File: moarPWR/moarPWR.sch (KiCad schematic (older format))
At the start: 0 parts

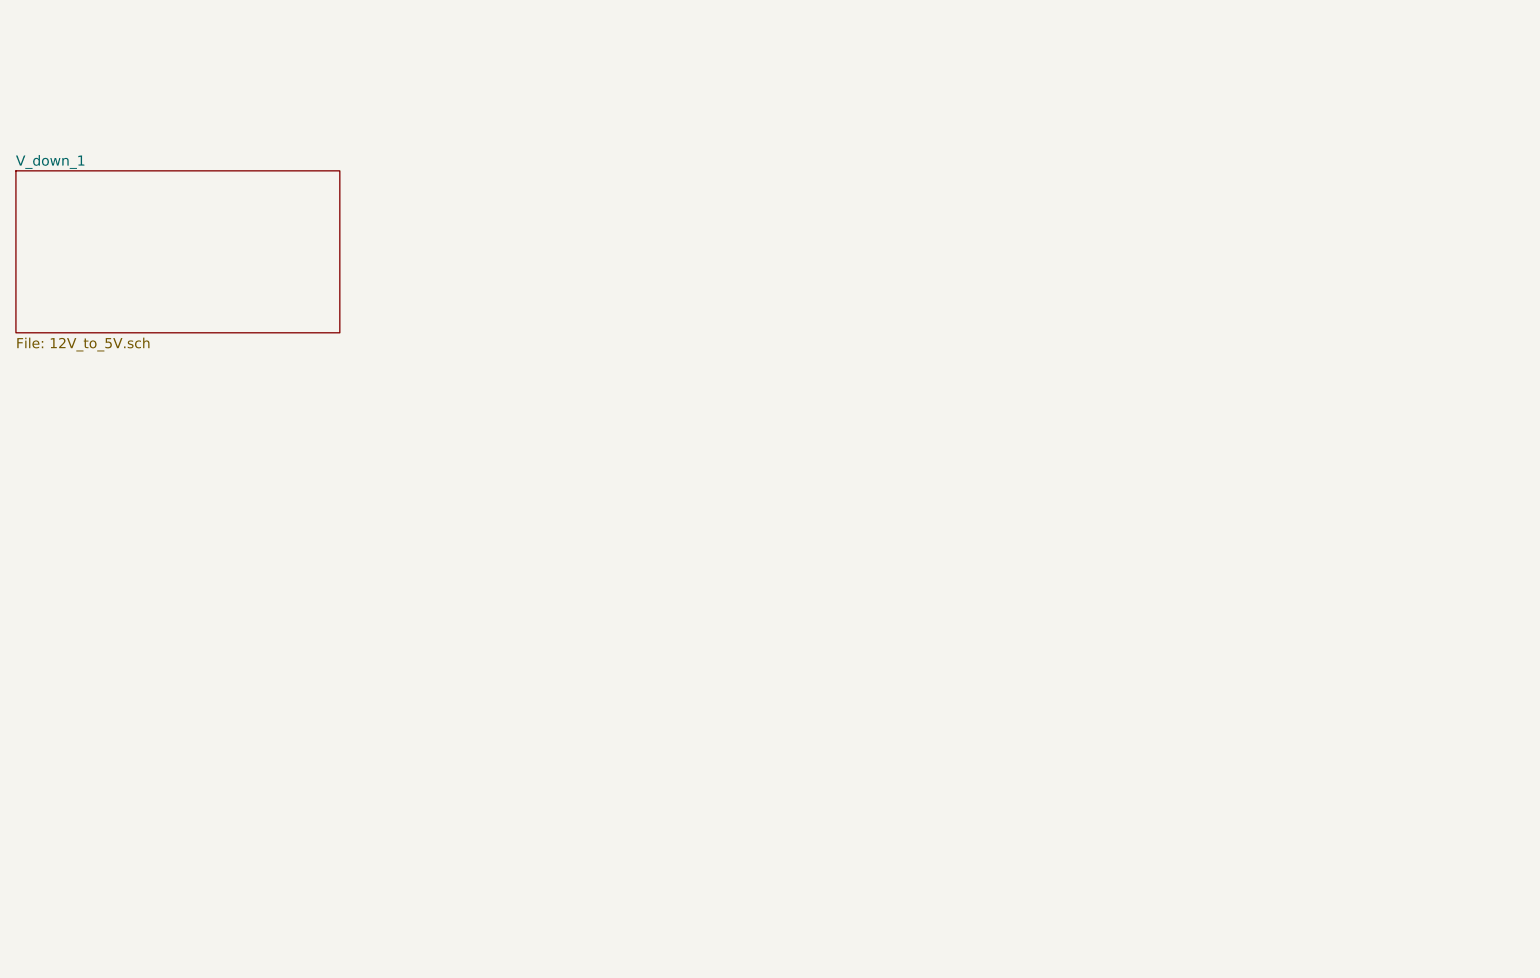
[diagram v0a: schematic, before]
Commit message: Added 5V stepdown skeleton and fleshed out top level sheet
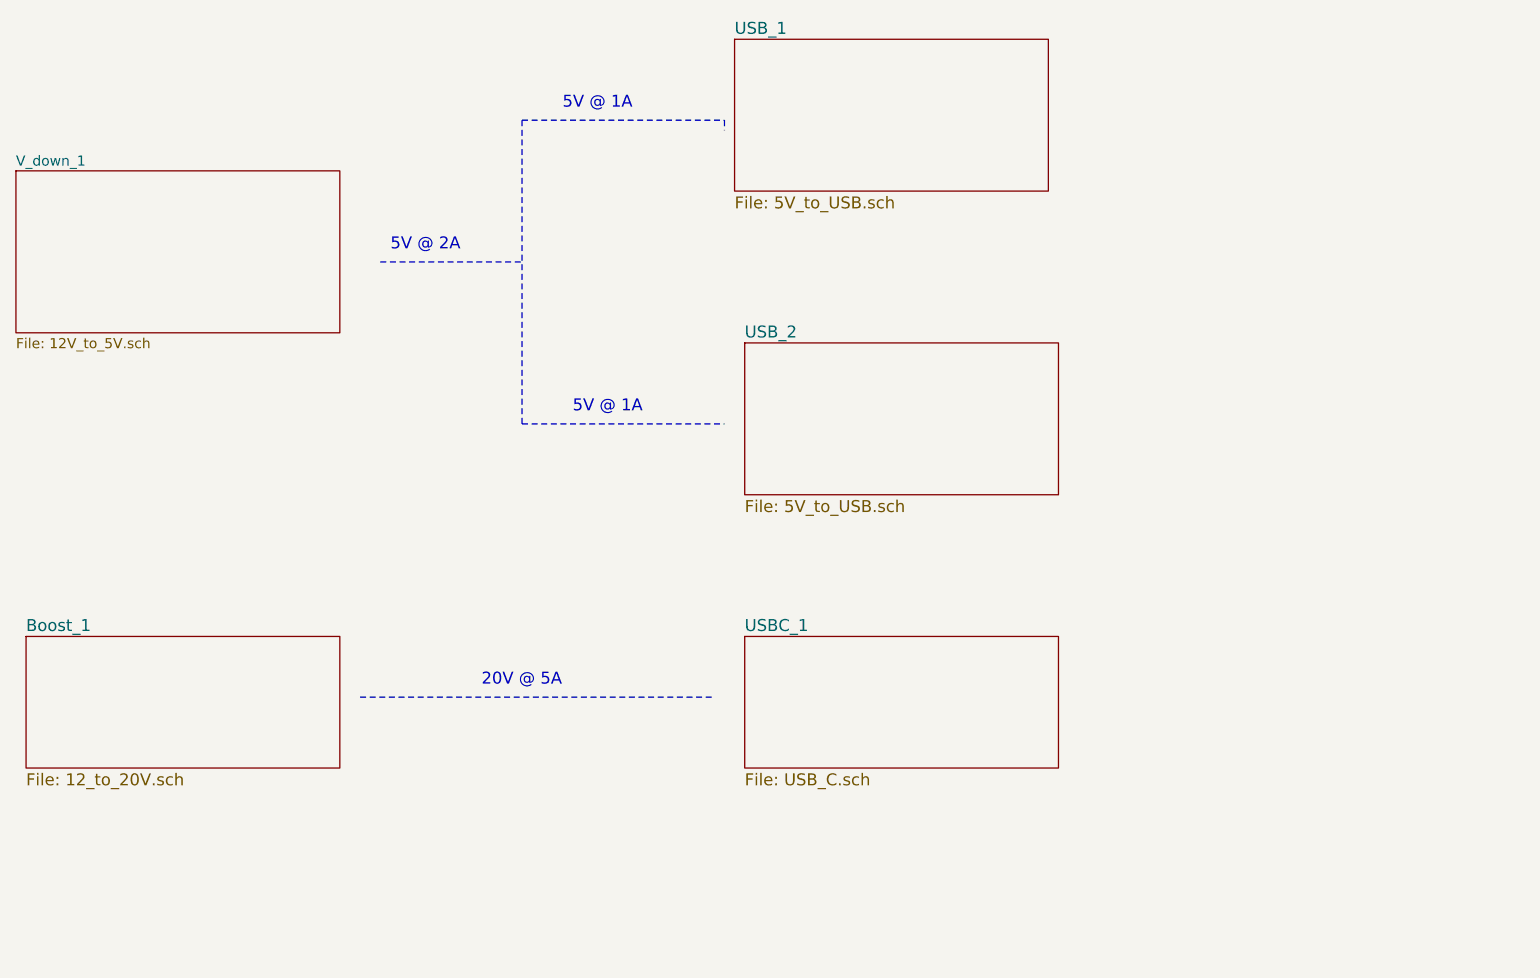
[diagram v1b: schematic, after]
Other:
- note added: "20V @ 5A"
- note added: "5V @ 1A"
- note added: "5V @ 2A"
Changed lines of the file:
@@
 EESchema Schematic File Version 4
+LIBS:moarPWR-cache
 EELAYER 26 0
 EELAYER END
 $Descr A4 11693 8268
 encoding utf-8
-Sheet 1 2
+Sheet 1 5
 Title "moarPWR"
 Date ""
@@
 F1 "12V_to_5V.sch" 50
 $EndSheet
+$Sheet
+S 5050 1850 1550 750
+U 5B5E9C4D
+F0 "USB_1" 59
+F1 "5V_to_USB.sch" 59
+$EndSheet
+$Sheet
+S 5100 3350 1550 750
+U 5B5E9C53
+F0 "USB_2" 59
+F1 "5V_to_USB.sch" 59
+$EndSheet
+Wire Notes Line
+	3300 2950 4000 2950
+Wire Notes Line
+	4000 2250 5000 2250
+Wire Notes Line
+	5000 2250 5000 2300
+Wire Notes Line
+	4000 3750 5000 3750
+Wire Notes Line
+	4000 2250 4000 3750
+$Sheet
+S 1550 4800 1550 650
+U 5B5E9CD0
+F0 "Boost_1" 59
+F1 "12_to_20V.sch" 59
+$EndSheet
+$Sheet
+S 5100 4800 1550 650
+U 5B5E9D28
+F0 "USBC_1" 59
+F1 "USB_C.sch" 59
+$EndSheet
+Wire Notes Line
+	3200 5100 4950 5100
+Text Notes 3350 2900 0    59   ~ 0
+5V @ 2A
+Text Notes 4200 2200 0    59   ~ 0
+5V @ 1A
+Text Notes 4250 3700 0    59   ~ 0
+5V @ 1A
+Text Notes 3800 5050 0    59   ~ 0
+20V @ 5A
 $EndSCHEMATC

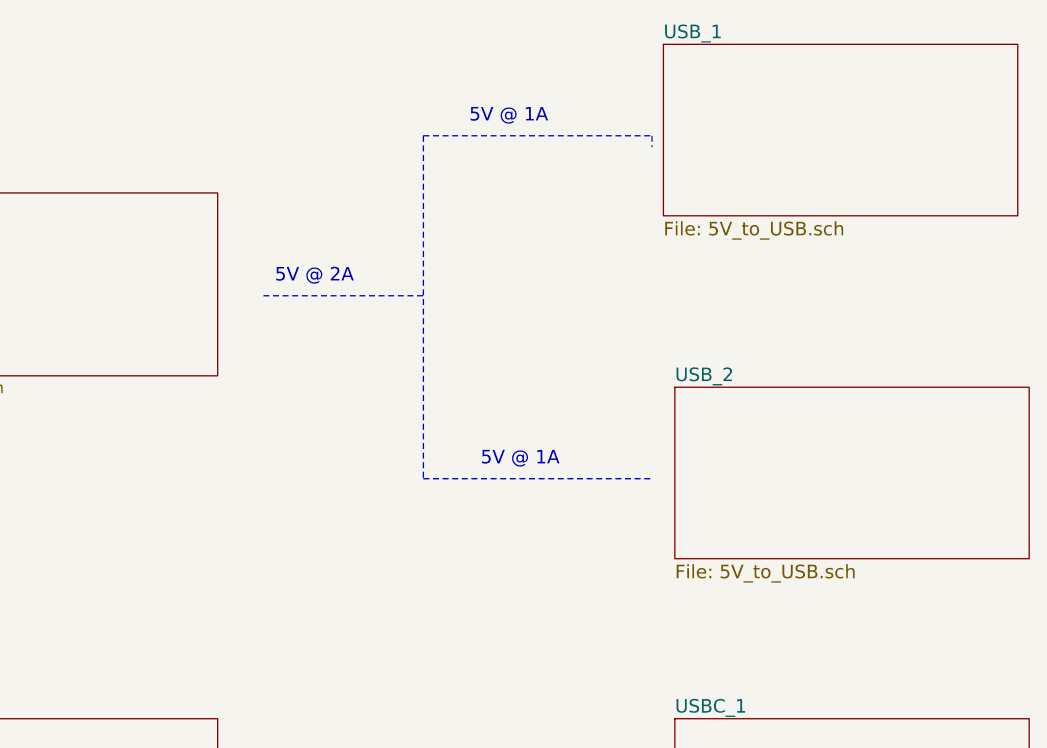
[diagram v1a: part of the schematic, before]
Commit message: Added port controller and power switch for 5V USB channels
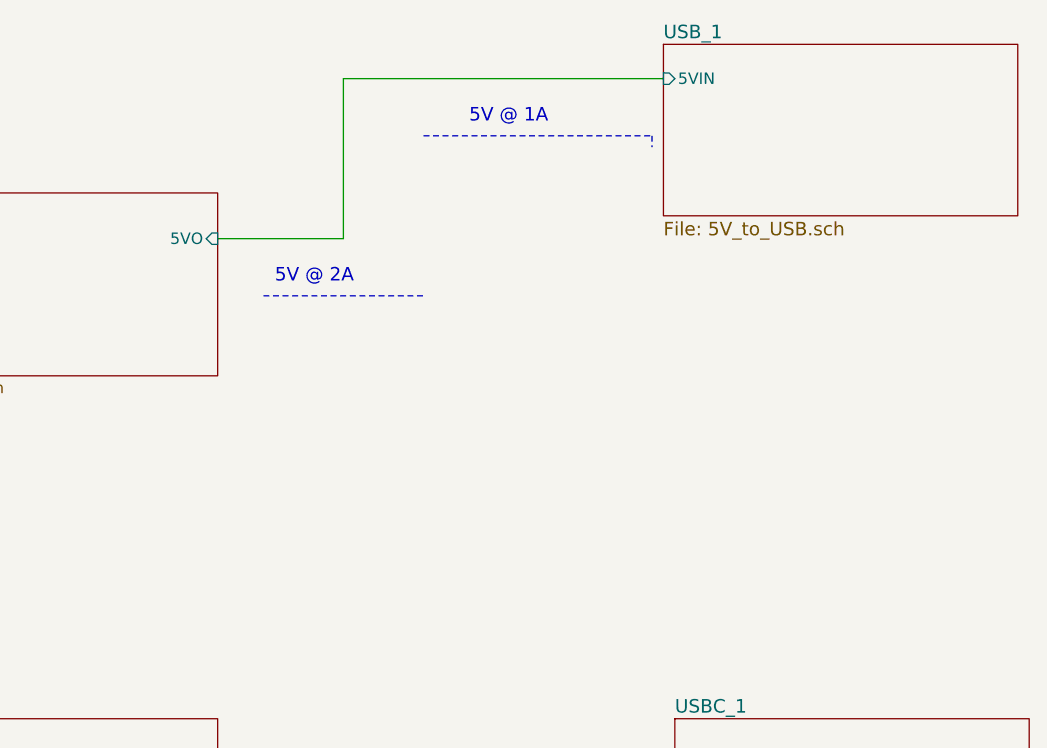
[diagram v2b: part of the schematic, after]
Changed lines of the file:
@@
 F0 "V_down_1" 50
 F1 "12V_to_5V.sch" 50
+F2 "5VO" I R 3100 2700 50
 $EndSheet
 $Sheet
@@
 F0 "USB_1" 59
 F1 "5V_to_USB.sch" 59
-$EndSheet
-$Sheet
-S 5100 3350 1550 750
-U 5B5E9C53
-F0 "USB_2" 59
-F1 "5V_to_USB.sch" 59
+F2 "5VIN" I L 5050 2000 50
 $EndSheet
 Wire Notes Line
@@
 Wire Notes Line
 	5000 2250 5000 2300
-Wire Notes Line
-	4000 3750 5000 3750
-Wire Notes Line
-	4000 2250 4000 3750
 $Sheet
 S 1550 4800 1550 650
@@
 Text Notes 4200 2200 0    59   ~ 0
 5V @ 1A
-Text Notes 4250 3700 0    59   ~ 0
-5V @ 1A
 Text Notes 3800 5050 0    59   ~ 0
 20V @ 5A
+Wire Wire Line
+	3100 2700 3650 2700
+Wire Wire Line
+	3650 2700 3650 2000
+Wire Wire Line
+	3650 2000 5050 2000
 $EndSCHEMATC

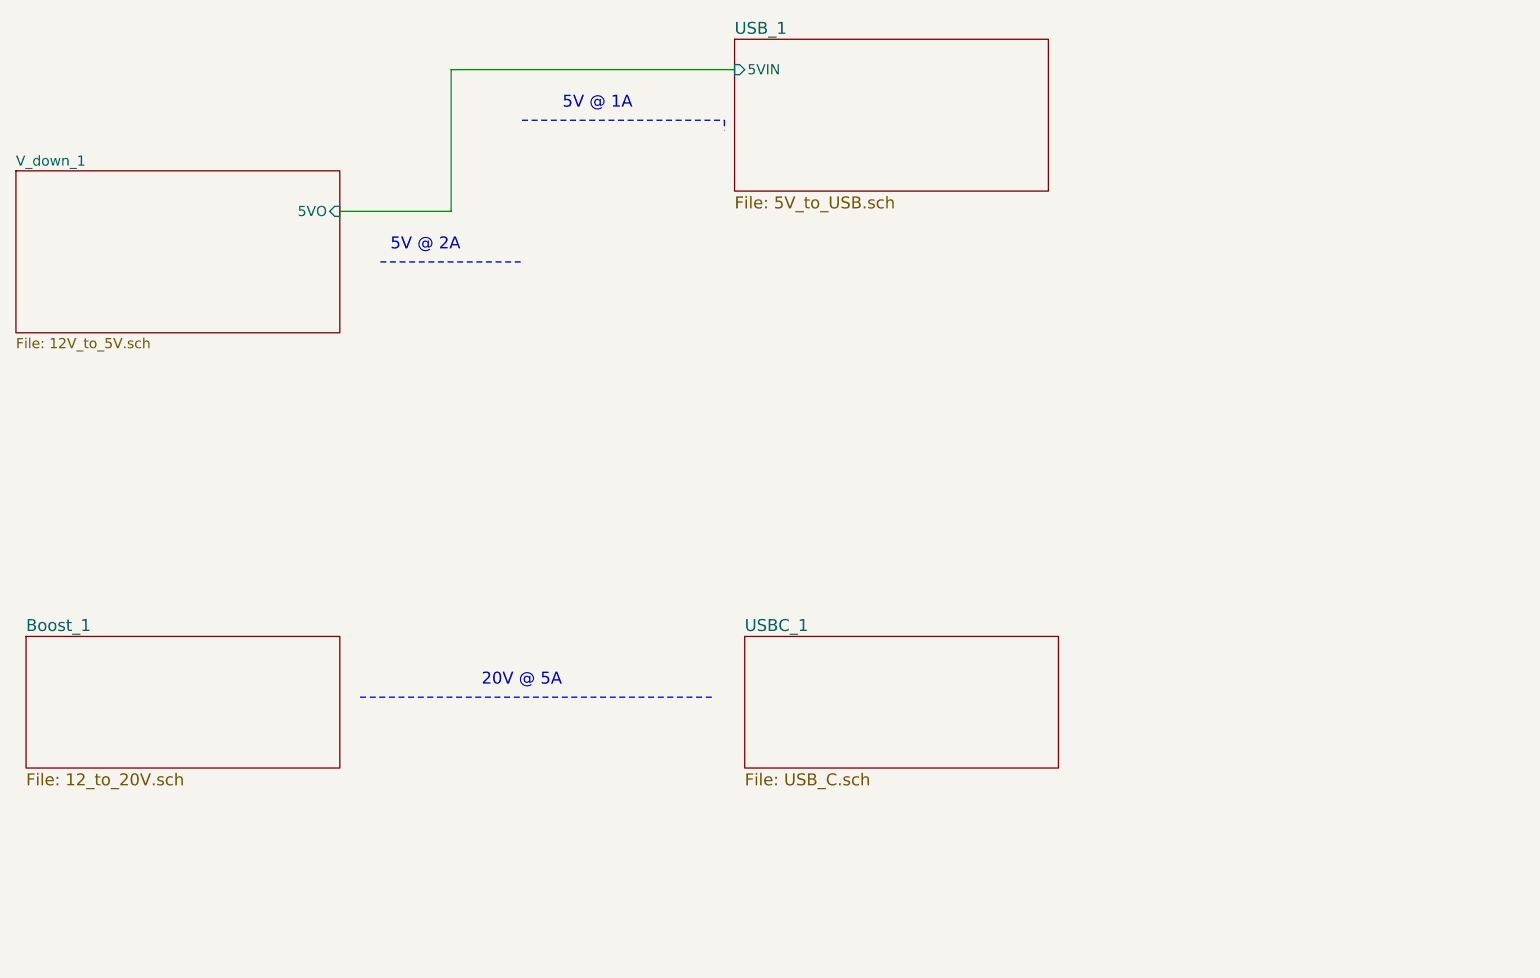
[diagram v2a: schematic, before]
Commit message: Updated part numbers in USB and display control. Added 7 Segment displays and driver.
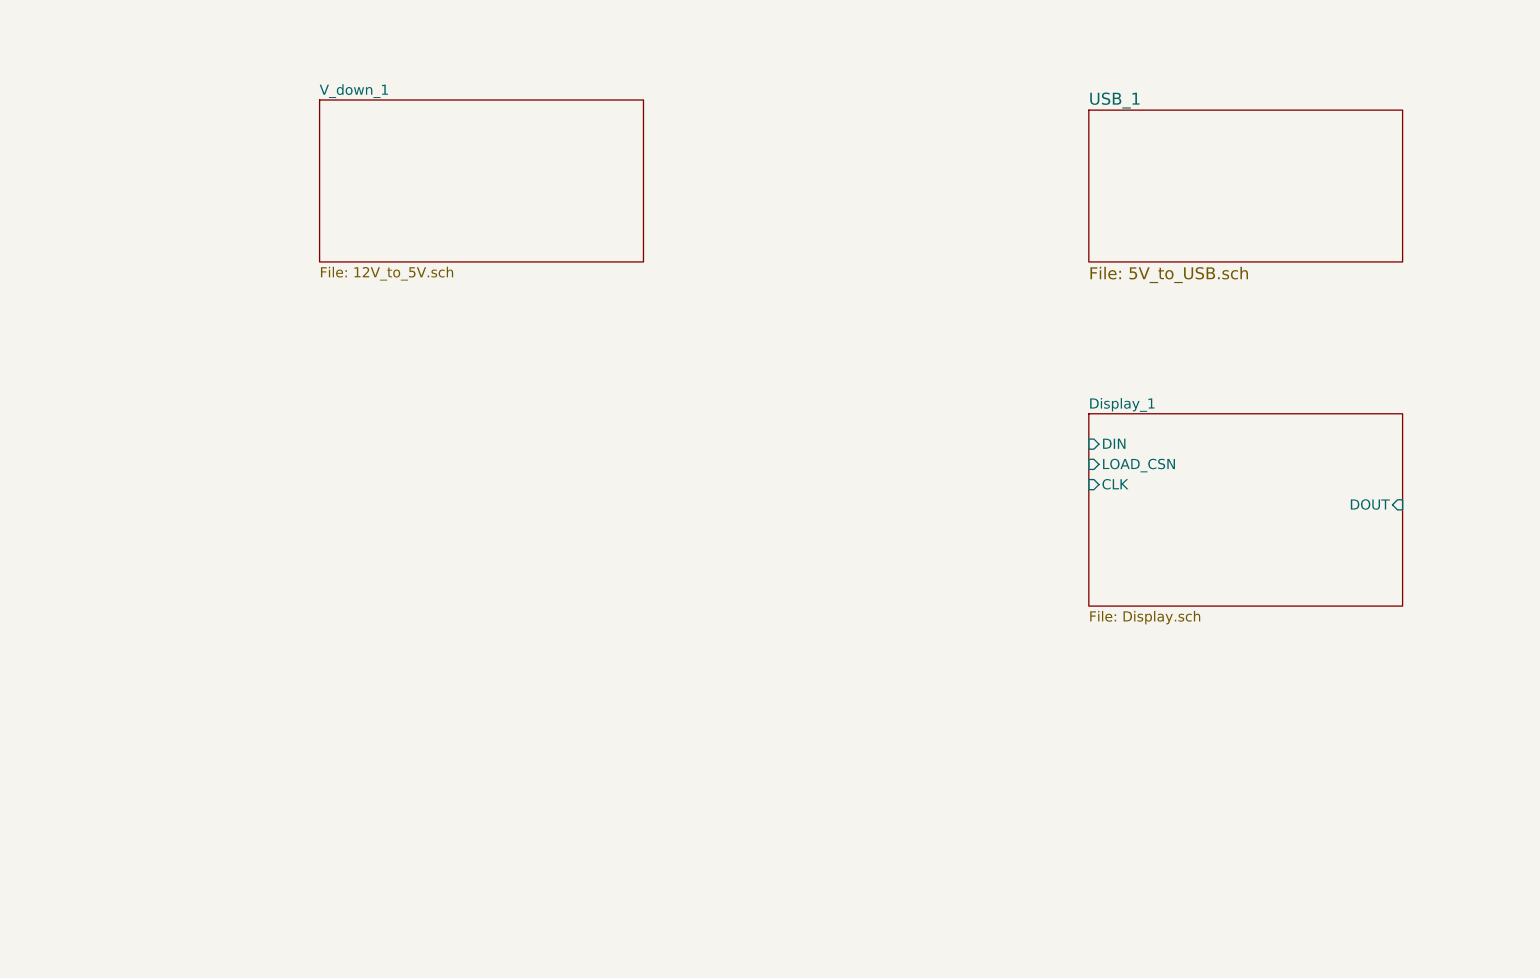
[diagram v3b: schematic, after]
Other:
- note removed: "20V @ 5A"
- note removed: "5V @ 1A"
- note removed: "5V @ 2A"
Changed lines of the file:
@@
 $Descr A4 11693 8268
 encoding utf-8
-Sheet 1 5
+Sheet 1 4
 Title "moarPWR"
 Date ""
@@
 $EndDescr
 $Sheet
-S 1500 2500 1600 800
+S 3000 2150 1600 800
 U 5B5D400A
 F0 "V_down_1" 50
 F1 "12V_to_5V.sch" 50
-F2 "5VO" I R 3100 2700 50
 $EndSheet
 $Sheet
-S 5050 1850 1550 750
+S 6800 2200 1550 750
 U 5B5E9C4D
 F0 "USB_1" 59
 F1 "5V_to_USB.sch" 59
-F2 "5VIN" I L 5050 2000 50
-$EndSheet
-Wire Notes Line
-	3300 2950 4000 2950
-Wire Notes Line
-	4000 2250 5000 2250
-Wire Notes Line
-	5000 2250 5000 2300
-$Sheet
-S 1550 4800 1550 650
-U 5B5E9CD0
-F0 "Boost_1" 59
-F1 "12_to_20V.sch" 59
 $EndSheet
 $Sheet
-S 5100 4800 1550 650
-U 5B5E9D28
-F0 "USBC_1" 59
-F1 "USB_C.sch" 59
+S 6800 3700 1550 950
+U 5BA57DA6
+F0 "Display_1" 50
+F1 "Display.sch" 50
+F2 "DIN" I L 6800 3850 50
+F3 "LOAD_CSN" I L 6800 3950 50
+F4 "CLK" I L 6800 4050 50
+F5 "DOUT" I R 8350 4150 50
 $EndSheet
-Wire Notes Line
-	3200 5100 4950 5100
-Text Notes 3350 2900 0    59   ~ 0
-5V @ 2A
-Text Notes 4200 2200 0    59   ~ 0
-5V @ 1A
-Text Notes 3800 5050 0    59   ~ 0
-20V @ 5A
-Wire Wire Line
-	3100 2700 3650 2700
-Wire Wire Line
-	3650 2700 3650 2000
-Wire Wire Line
-	3650 2000 5050 2000
 $EndSCHEMATC

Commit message: Added MSP and current sense amplifier
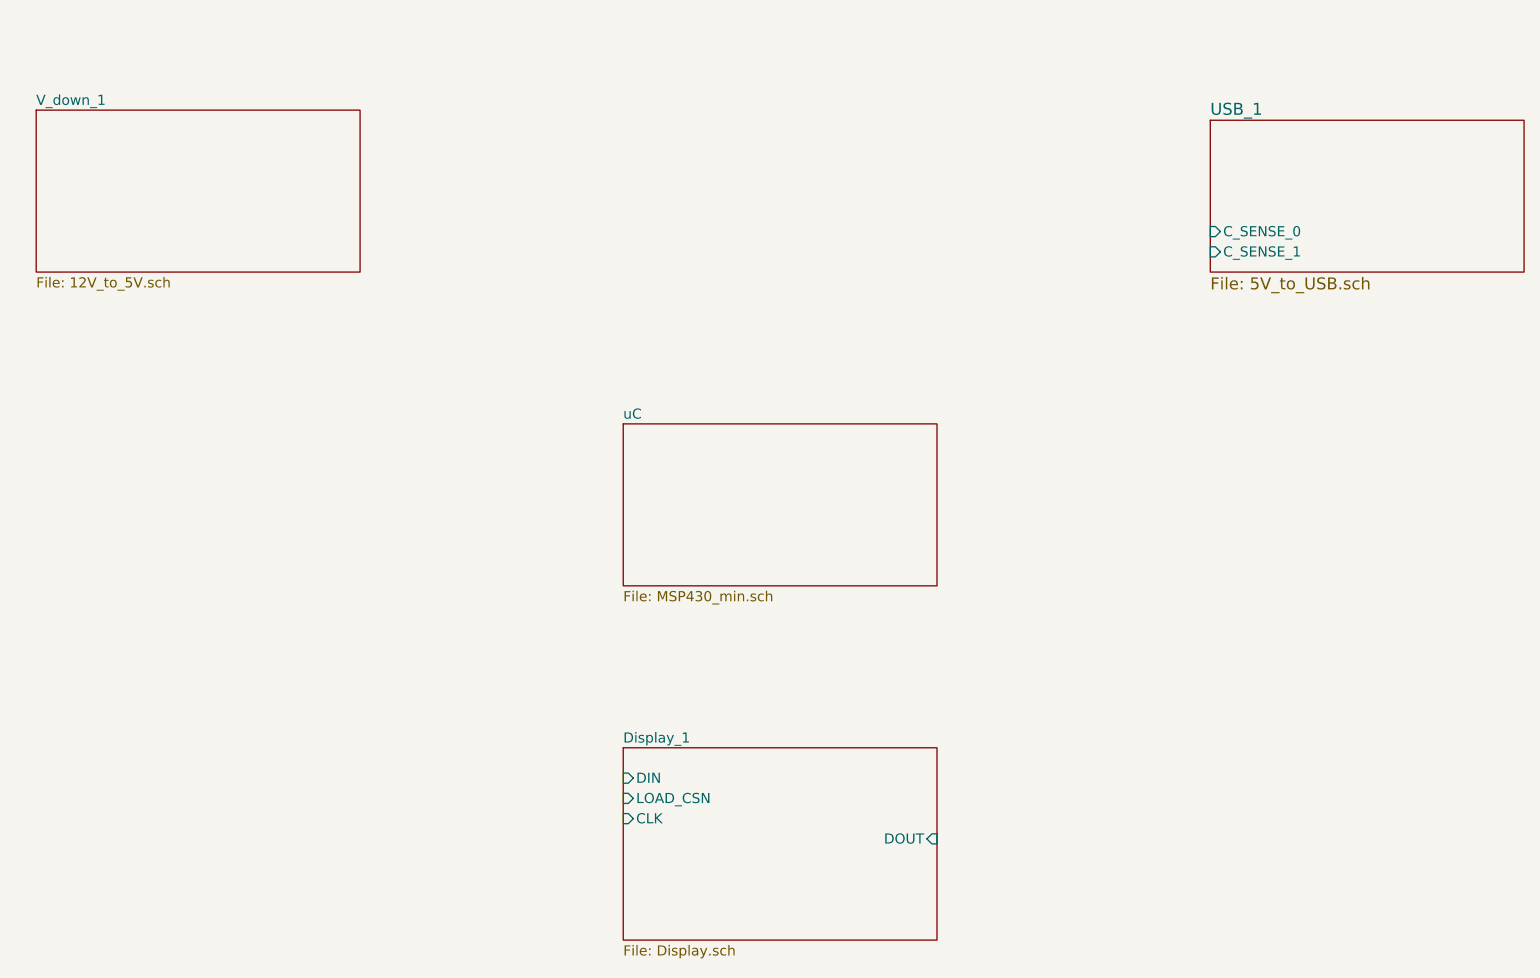
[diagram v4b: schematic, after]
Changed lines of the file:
@@
 $Descr A4 11693 8268
 encoding utf-8
-Sheet 1 4
+Sheet 1 5
 Title "moarPWR"
 Date ""
@@
 $EndDescr
 $Sheet
-S 3000 2150 1600 800
+S 1600 2200 1600 800
 U 5B5D400A
 F0 "V_down_1" 50
@@
 $EndSheet
 $Sheet
-S 6800 2200 1550 750
+S 7400 2250 1550 750
 U 5B5E9C4D
 F0 "USB_1" 59
 F1 "5V_to_USB.sch" 59
+F2 "C_SENSE_0" I L 7400 2800 50
+F3 "C_SENSE_1" I L 7400 2900 50
 $EndSheet
 $Sheet
-S 6800 3700 1550 950
+S 4500 5350 1550 950
 U 5BA57DA6
 F0 "Display_1" 50
 F1 "Display.sch" 50
-F2 "DIN" I L 6800 3850 50
-F3 "LOAD_CSN" I L 6800 3950 50
-F4 "CLK" I L 6800 4050 50
-F5 "DOUT" I R 8350 4150 50
+F2 "DIN" I L 4500 5500 50
+F3 "LOAD_CSN" I L 4500 5600 50
+F4 "CLK" I L 4500 5700 50
+F5 "DOUT" I R 6050 5800 50
+$EndSheet
+$Sheet
+S 4500 3750 1550 800
+U 5C623F3F
+F0 "uC" 50
+F1 "MSP430_min.sch" 50
 $EndSheet
 $EndSCHEMATC
